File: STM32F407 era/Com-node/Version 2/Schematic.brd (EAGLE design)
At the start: 127 x 165.1 mm, 73 parts, among them IC2 lm2575, Q2 12MHz, Q3 12MHz, U1 MAX13052ESA+, U2 SMS05, U3 MAX232AEWE+, X1 SDBMF, X5 679105700

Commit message: OPT2 til GND på gamma
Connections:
- net GND: now also U$32.P$14
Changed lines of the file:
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@@
 <contactref element="U$18" pad="22"/>
 <contactref element="U$18" pad="16"/>
+<contactref element="U$32" pad="P$14"/>
 </signal>
 <signal name="3.3V">
@@
 </signal>
 </signals>
-<errors>
-</errors>
 </board>
 </drawing>

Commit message: work work
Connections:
- net GND: now also U$18.25; no longer U$18.19
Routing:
- net V-SENSE: track 45.9 -> 39.7 mm, vias 1 -> 2
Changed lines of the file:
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@@
 <wire x1="80.0575" y1="32.655" x2="80.3275" y2="32.385" width="0.4064" layer="1"/>
 <via x="80.3275" y="32.385" extent="1-16" drill="0.381"/>
-<wire x1="80.3275" y1="32.385" x2="80.3275" y2="59.055" width="0.4064" layer="16"/>
-<wire x1="80.3275" y1="59.055" x2="82.2325" y2="60.96" width="0.4064" layer="16"/>
-<wire x1="82.2325" y1="60.96" x2="93.2633" y2="60.96" width="0.4064" layer="16"/>
-<wire x1="93.2633" y1="60.96" x2="96.1502" y2="63.8469" width="0.4064" layer="16"/>
+<wire x1="80.3275" y1="32.385" x2="80.3275" y2="35.56" width="0.4064" layer="16"/>
+<via x="80.3275" y="35.56" extent="1-16" drill="0.381"/>
+<wire x1="80.3275" y1="35.56" x2="80.3275" y2="48.5775" width="0.4064" layer="1"/>
+<wire x1="80.3275" y1="48.5775" x2="94.2975" y2="62.5475" width="0.4064" layer="1"/>
+<wire x1="94.2975" y1="62.5475" x2="94.8508" y2="62.5475" width="0.4064" layer="1"/>
+<wire x1="94.8508" y1="62.5475" x2="96.1502" y2="63.8469" width="0.4064" layer="1"/>
 </signal>
 <signal name="DEBUG-LED2">
@@
 <contactref element="LED1" pad="C"/>
 <contactref element="LED4" pad="C"/>
-<contactref element="U$18" pad="19"/>
 <contactref element="U$18" pad="2"/>
 <contactref element="U$18" pad="21"/>
@@
 <contactref element="U$18" pad="16"/>
 <contactref element="U$32" pad="P$14"/>
+<contactref element="U$18" pad="25"/>
 </signal>
 <signal name="3.3V">

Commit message: adding last changes to accomendate changes in H-Bridge
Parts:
- added PTC1: (no value), microbuilder:PTC1812
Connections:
- new net N$57: C7.+, IC2.1, PTC1.P$1, R12.1
- net 12V: now also PTC1.P$2; no longer C7.+, IC2.1, R12.1
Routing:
- net N$57: track 0.00 -> 30.7 mm
- net 12V: track 40.2 -> 22.0 mm
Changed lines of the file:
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@@
 <attribute name="VALUE" x="70.231" y="95.1865" size="0.4064" layer="27" ratio="10" rot="R90"/>
 </element>
+<element name="PTC1" library="microbuilder" package="PTC1812" value="" x="74.93" y="4.7625" rot="R270"/>
 </elements>
 <signals>
@@
 </signal>
 <signal name="12V">
-<contactref element="IC2" pad="1"/>
-<contactref element="C7" pad="+"/>
-<wire x1="74.93" y1="13.97" x2="69.215" y2="13.97" width="1.016" layer="1"/>
-<wire x1="69.215" y1="13.97" x2="69.215" y2="14.5923" width="1.016" layer="1"/>
-<wire x1="69.215" y1="14.5923" x2="69.1261" y2="14.6812" width="1.016" layer="1"/>
-<contactref element="R12" pad="1"/>
-<wire x1="74.93" y1="13.97" x2="78.105" y2="17.145" width="0.4064" layer="1"/>
-<wire x1="78.105" y1="17.145" x2="78.105" y2="26.67" width="0.4064" layer="1"/>
-<wire x1="78.105" y1="26.67" x2="77.1525" y2="27.6225" width="0.4064" layer="1"/>
-<wire x1="77.1525" y1="27.6225" x2="77.1525" y2="29.4005" width="0.4064" layer="1"/>
 <contactref element="U$18" pad="26"/>
-<wire x1="90.2575" y1="10.7875" x2="78.1125" y2="10.7875" width="1.016" layer="1"/>
-<wire x1="78.1125" y1="10.7875" x2="74.93" y2="13.97" width="1.016" layer="1"/>
+<contactref element="PTC1" pad="P$2"/>
+<wire x1="90.2575" y1="10.7875" x2="79.685" y2="10.7875" width="1.016" layer="1"/>
+<wire x1="79.685" y1="10.7875" x2="78.105" y2="9.2075" width="1.016" layer="1"/>
+<wire x1="78.105" y1="9.2075" x2="78.105" y2="3.4925" width="1.016" layer="1"/>
+<wire x1="78.105" y1="3.4925" x2="77.275" y2="2.6625" width="1.016" layer="1"/>
+<wire x1="77.275" y1="2.6625" x2="74.93" y2="2.6625" width="1.016" layer="1"/>
 </signal>
 <signal name="COMRX">
@@
 <wire x1="72.0725" y1="93.7895" x2="72.0725" y2="95.9765" width="0.4064" layer="1"/>
 </signal>
+<signal name="N$57">
+<contactref element="IC2" pad="1"/>
+<contactref element="C7" pad="+"/>
+<contactref element="R12" pad="1"/>
+<wire x1="74.93" y1="13.97" x2="69.215" y2="13.97" width="1.016" layer="1"/>
+<wire x1="69.215" y1="13.97" x2="69.215" y2="14.5923" width="1.016" layer="1"/>
+<wire x1="69.215" y1="14.5923" x2="69.1261" y2="14.6812" width="1.016" layer="1"/>
+<wire x1="74.93" y1="13.97" x2="78.105" y2="17.145" width="0.4064" layer="1"/>
+<wire x1="78.105" y1="17.145" x2="78.105" y2="26.67" width="0.4064" layer="1"/>
+<wire x1="78.105" y1="26.67" x2="77.1525" y2="27.6225" width="0.4064" layer="1"/>
+<wire x1="77.1525" y1="27.6225" x2="77.1525" y2="29.4005" width="0.4064" layer="1"/>
+<contactref element="PTC1" pad="P$1"/>
+<wire x1="74.93" y1="13.97" x2="74.93" y2="6.8625" width="1.016" layer="1"/>
+</signal>
 </signals>

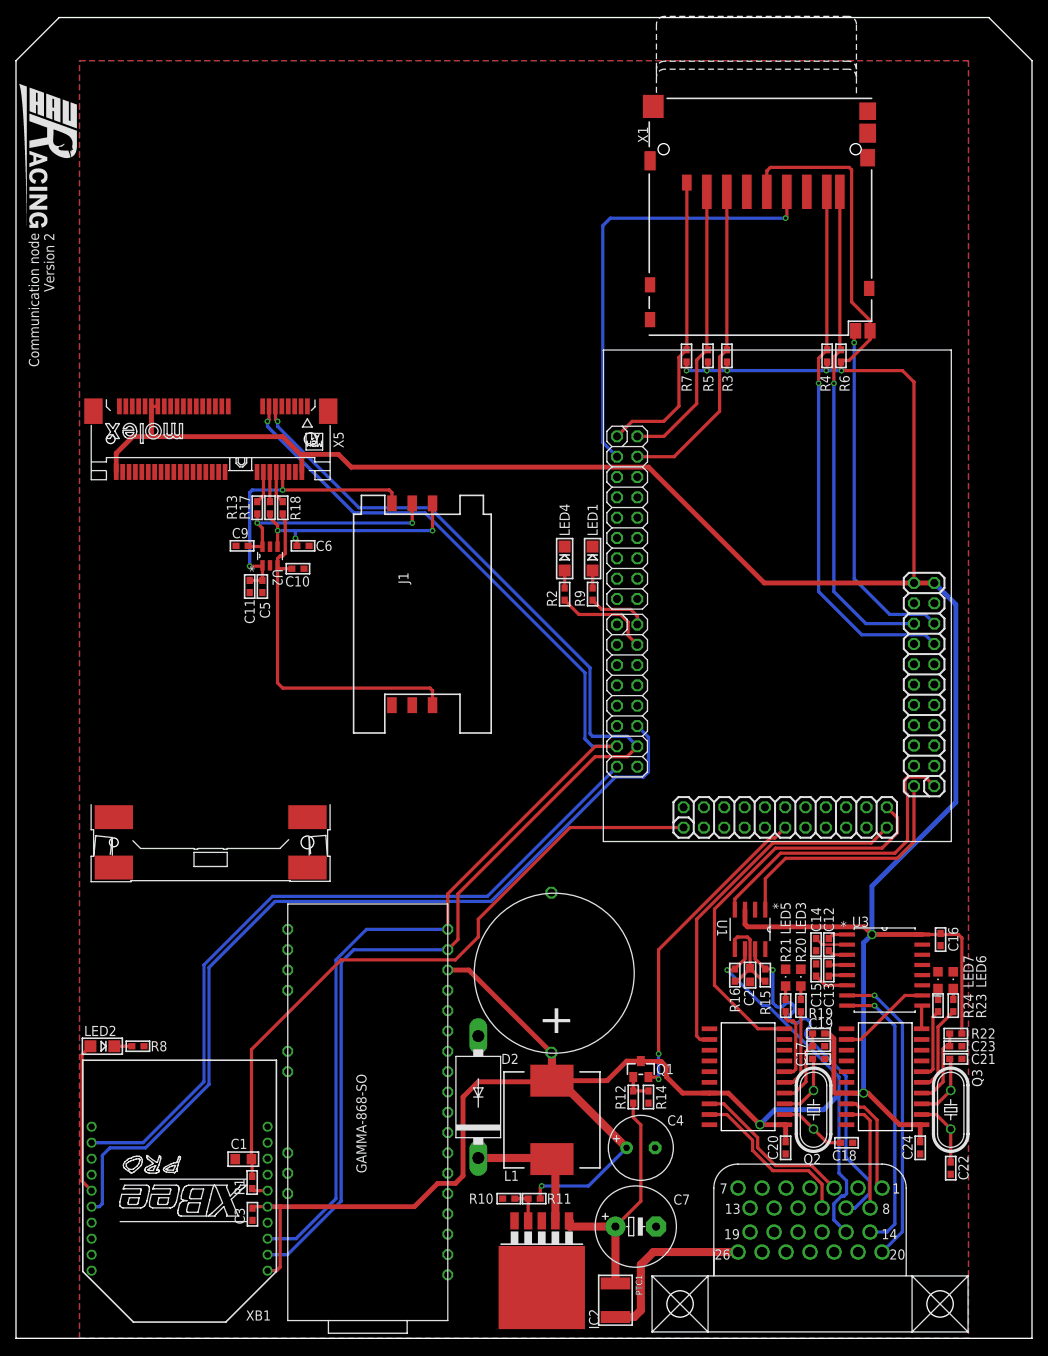
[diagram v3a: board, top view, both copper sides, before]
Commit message: added 4 16MBit SPI flash for SD card backup
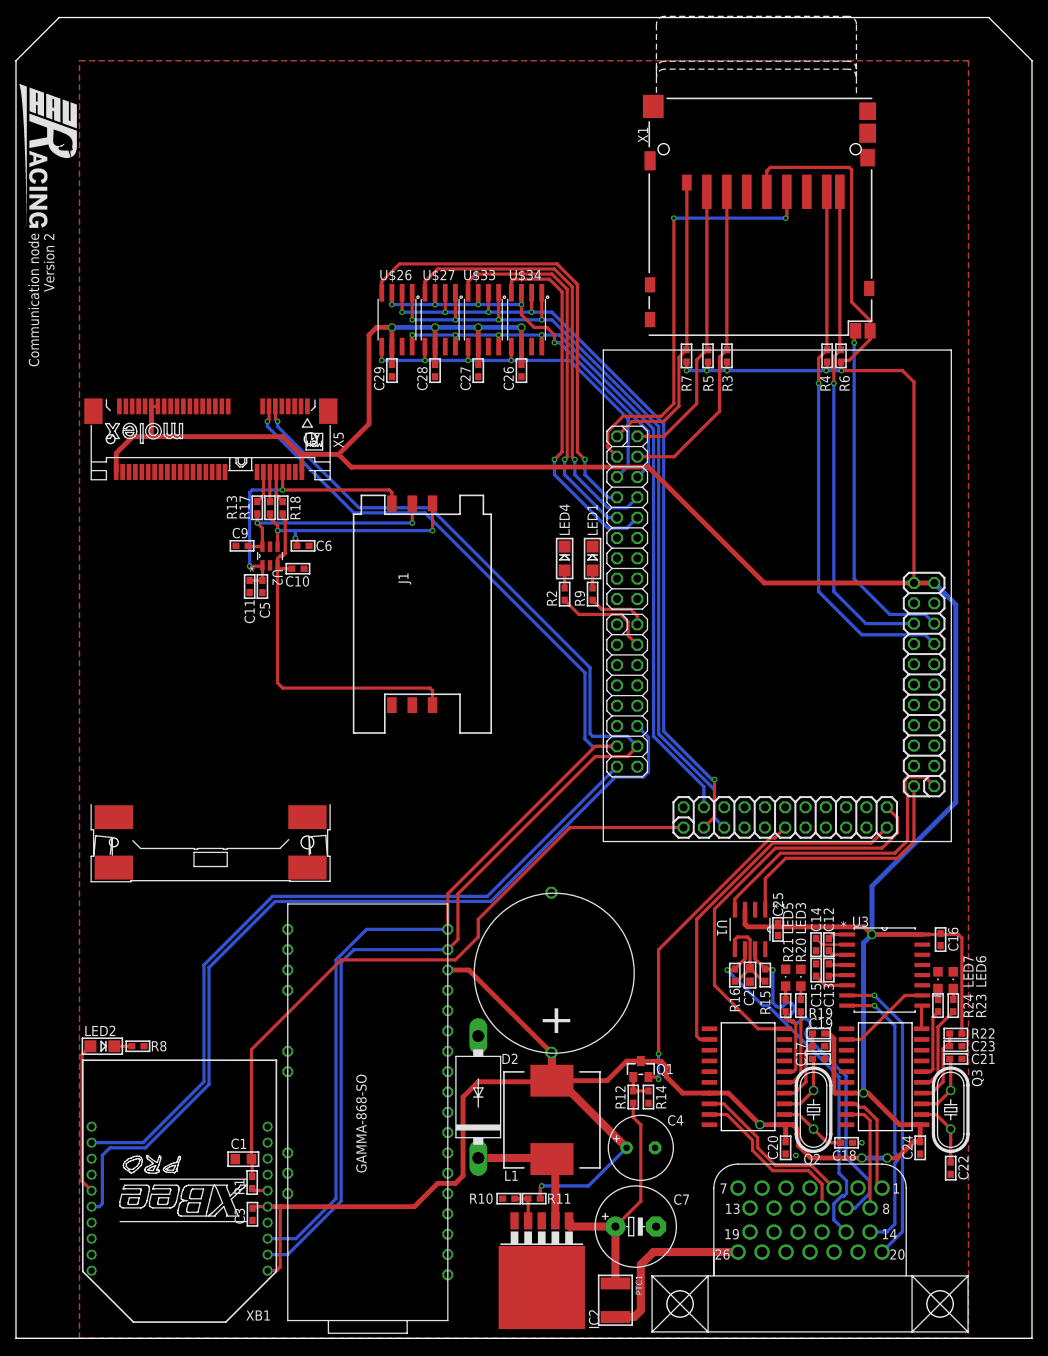
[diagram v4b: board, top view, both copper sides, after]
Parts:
- added C25, C26, C27, C28, C29: 100nF, microbuilder:_0603
- added U$26, U$27, U$33, U$34: AT45DB161D, SparkFun-DigitalIC:SO08-EIAJ
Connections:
- new net CS1: U$1.P$51, U$26.4
- new net CS2: U$1.P$52, U$27.4
- new net CS3: U$1.P$53, U$33.4
- new net CS4: U$1.P$54, U$34.4
- new net MISO: U$1.P$4, U$26.8, U$27.8, U$33.8, U$34.8
- new net MOSI: U$1.P$5, U$26.1, U$27.1, U$33.1, U$34.1
- new net RESET: U$1.P$50, U$26.3, U$27.3, U$33.3, U$34.3
- new net SCK: U$1.P$3, U$26.2, U$27.2, U$33.2, U$34.2
- new net WP: U$1.P$49, U$26.5, U$27.5, U$33.5, U$34.5
- net 3.3V: now also C25.2, C26.2, C27.2, C28.2, C29.2, U$26.6, U$27.6, U$33.6, U$34.6
- net GND: now also C25.1, C26.1, C27.1, C28.1, C29.1, U$26.7, U$27.7, U$33.7, U$34.7
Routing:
- net MOSI: track 0.00 -> 103.4 mm, vias 0 -> 4
- net SCK: track 0.00 -> 102.0 mm, vias 0 -> 5
- net MISO: track 0.00 -> 90.7 mm, vias 0 -> 4
- net 3.3V: track 512.4 -> 573.3 mm, vias 9 -> 15
- net CS1: track 0.00 -> 57.2 mm, vias 0 -> 1
- net CS2: track 0.00 -> 55.1 mm, vias 0 -> 1
- net RESET: track 0.00 -> 52.1 mm, vias 0 -> 5
- net WP: track 0.00 -> 48.6 mm, vias 0 -> 4
- net CS3: track 0.00 -> 47.0 mm, vias 0 -> 1
- net CS4: track 0.00 -> 45.4 mm, vias 0 -> 1
- net SDIO_SCK: track 56.2 -> 53.8 mm, vias 1 -> 2
